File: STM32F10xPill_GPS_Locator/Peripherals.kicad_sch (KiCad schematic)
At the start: 0 parts

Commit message: Add controller and clocks
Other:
- company: (none) -> MTP
- title: (none) -> STM32F100C4T6B GPS Locator
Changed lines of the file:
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@@
 	(generator "eeschema")
 	(generator_version "9.0")
-	(paper "A4")
+	(paper "A3")
+	(title_block
+		(title "STM32F100C4T6B GPS Locator")
+		(date "2025-03-06")
+		(rev "1.0.0")
+		(company "MTP")
+	)
 )

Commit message: Add library parts for peripherals
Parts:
- added U2: QMC5883P, Package_LGA:LGA-16_3x3mm_P0.5mm, symbol ICs:QMC5883P
- added U4: ATGM336H-5N31, ICs:ATGM336H_SMD_9.7x10.1mm, symbol ICs:ATGM336H
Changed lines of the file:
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@@
 		(company "MTP")
 	)
+	(symbol
+		(lib_id "ICs:ATGM336H")
+		(at 257.81 135.89 0)
+		(unit 1)
+		(exclude_from_sim no)
+		(in_bom yes)
+		(on_board yes)
+		(dnp no)
+		(property "Reference" "U4"
+			(at 263.144 112.522 0)
+			(do_not_autoplace yes)
+			(effects
+				(font
+					(size 1.27 1.27)
+				)
+			)
+		)
+		(property "Value" "ATGM336H-5N31"
+			(at 268.732 114.3 0)
+			(effects
+				(font
+					(size 1.27 1.27)
+				)
+			)
+		)
+		(property "Footprint" "ICs:ATGM336H_SMD_9.7x10.1mm"
+			(at 257.81 135.89 0)
+			(effects
+				(font
+					(size 1.27 1.27)
+				)
+				(hide yes)
+			)
+		)
+		(property "Datasheet" ""
+			(at 257.81 135.89 0)
+			(effects
+				(font
+					(size 1.27 1.27)
+				)
+				(hide yes)
+			)
+		)
+		(property "Description" ""
+			(at 257.81 135.89 0)
+			(effects
+				(font
+					(size 1.27 1.27)
+				)
+				(hide yes)
+			)
+		)
+		(property "LCSC Part" "C90770"
+			(at 257.81 135.89 0)
+			(effects
+				(font
+					(size 1.27 1.27)
+				)
+				(hide yes)
+			)
+		)
+		(pin "9"
+		)
+		(pin "17"
+		)
+		(pin "8"
+		)
+		(pin "14"
+		)
+		(pin "16"
+		)
+		(pin "6"
+		)
+		(pin "4"
+		)
+		(pin "3"
+		)
+		(pin "1"
+		)
+		(pin "12"
+		)
+		(pin "11"
+		)
+		(pin "3"
+		)
+		(pin "2"
+		)
+		(pin "10"
+		)
+		(instances
+			(project ""
+				(path "/ea8b3ef8-8ecc-4b82-8187-a133f9b3c76f/fb7f8d9c-e54d-452d-9b35-e091bd157ab7"
+					(reference "U4")
+					(unit 1)
+				)
+			)
+		)
+	)
+	(symbol
+		(lib_id "ICs:QMC5883P")
+		(at 148.59 132.08 0)
+		(unit 1)
+		(exclude_from_sim no)
+		(in_bom yes)
+		(on_board yes)
+		(dnp no)
+		(property "Reference" "U2"
+			(at 153.67 118.872 0)
+			(effects
+				(font
+					(size 1.27 1.27)
+				)
+			)
+		)
+		(property "Value" "QMC5883P"
+			(at 156.972 120.65 0)
+			(effects
+				(font
+					(size 1.27 1.27)
+				)
+			)
+		)
+		(property "Footprint" "Package_LGA:LGA-16_3x3mm_P0.5mm"
+			(at 148.59 132.08 0)
+			(effects
+				(font
+					(size 1.27 1.27)
+				)
+				(hide yes)
+			)
+		)
+		(property "Datasheet" ""
+			(at 148.59 132.08 0)
+			(effects
+				(font
+					(size 1.27 1.27)
+				)
+				(hide yes)
+			)
+		)
+		(property "Description" ""
+			(at 148.59 132.08 0)
+			(effects
+				(font
+					(size 1.27 1.27)
+				)
+				(hide yes)
+			)
+		)
+		(property "LCSC Part" "C2847467"
+			(at 148.59 132.08 0)
+			(effects
+				(font
+					(size 1.27 1.27)
+				)
+				(hide yes)
+			)
+		)
+		(pin "11"
+		)
+		(pin "1"
+		)
+		(pin "9"
+		)
+		(pin "10"
+		)
+		(pin "2"
+		)
+		(pin "16"
+		)
+		(instances
+			(project ""
+				(path "/ea8b3ef8-8ecc-4b82-8187-a133f9b3c76f/fb7f8d9c-e54d-452d-9b35-e091bd157ab7"
+					(reference "U2")
+					(unit 1)
+				)
+			)
+		)
+	)
 )

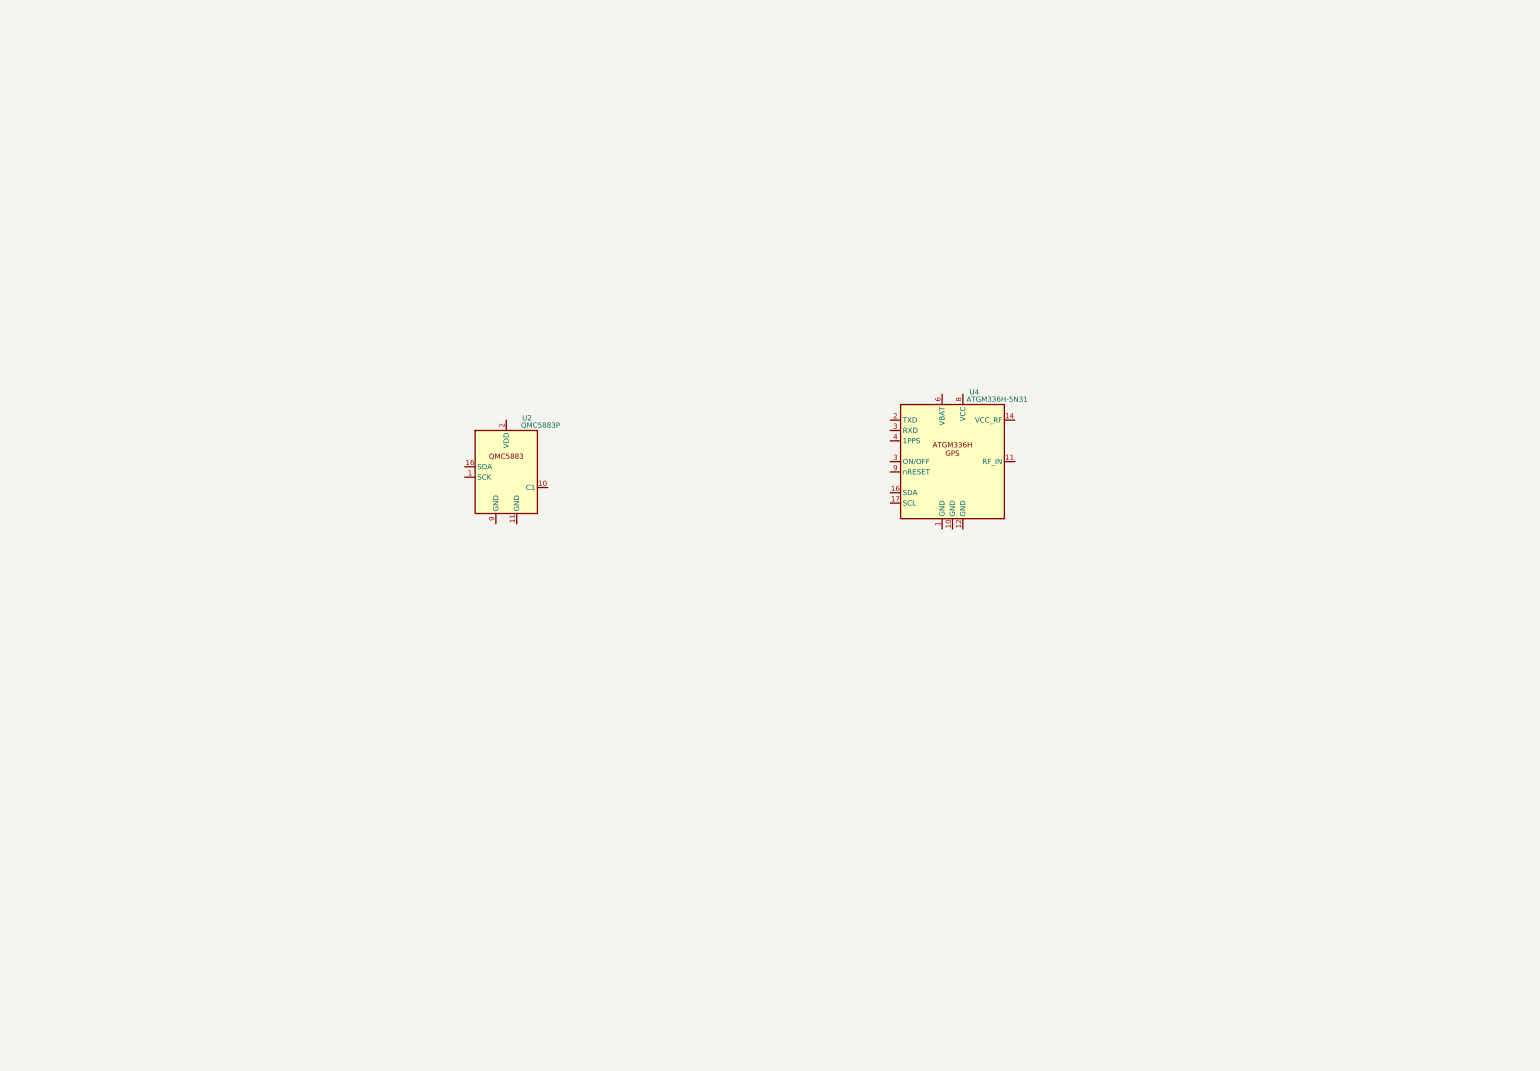
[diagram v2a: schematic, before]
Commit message: Work on adding GPS and Compass Peripherals
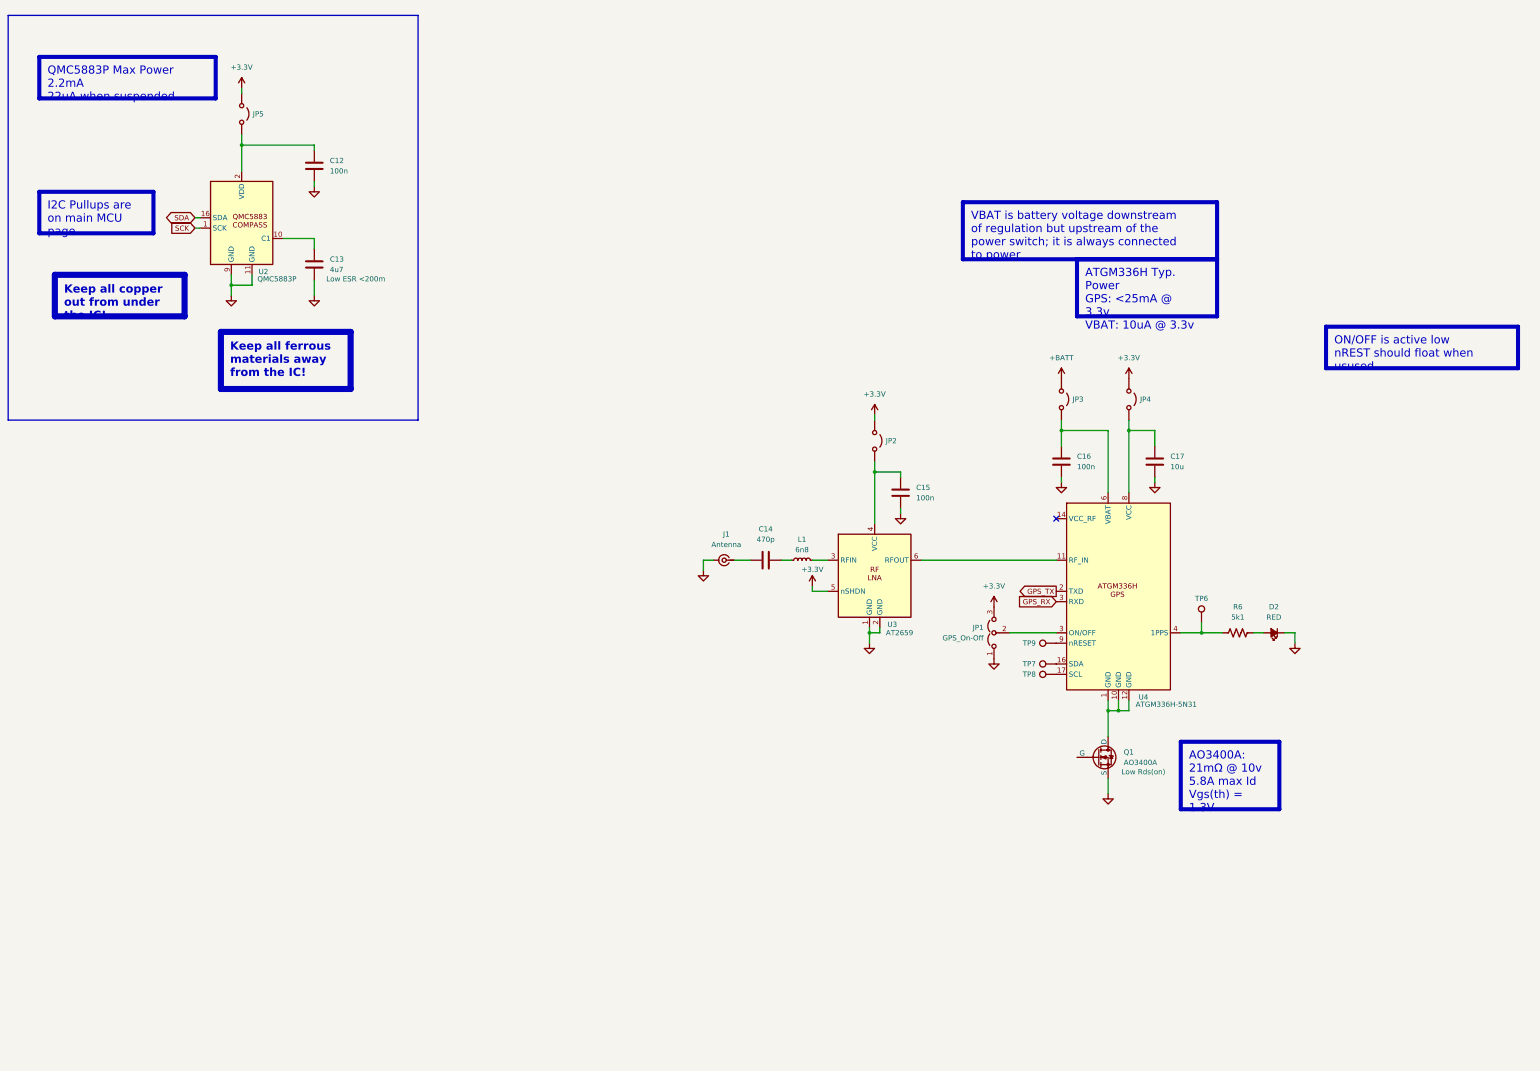
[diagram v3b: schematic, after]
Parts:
- added C12, C15, C16: 100n, symbol Device:C
- added C13: 4u7, symbol Device:C
- added C14: 470p, symbol Device:C
- added C17: 10u, symbol Device:C
- added D2: RED, symbol Device:LED_Small_Filled
- added J1: Antenna, Connector_Coaxial:U.FL_Molex_MCRF_73412-0110_Vertical, symbol Connector:Conn_Coaxial_Small
- added JP1: GPS_On-Off, symbol Jumper:Jumper_3_Open
- added JP2, JP3, JP4, JP5: Jumper_2_Open, symbol Jumper:Jumper_2_Open
- added L1: 6n8, symbol Device:L_Small
- added Q1: AO3400A, symbol Simulation_SPICE:NMOS
- added R6: 5k1, symbol Device:R_US
- added TP6: GPS_1PPS, symbol Connector:TestPoint
- added TP7, TP8: GPS_SDA, symbol Connector:TestPoint
- added TP9: GPS_nRESET, symbol Connector:TestPoint
- added U3: AT2659, Package_DFN_QFN:DFN-6_1.6x1.3mm_P0.4mm, symbol ICs:AT2659
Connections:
- net at U4.1 (GND): now also U4.10 (GND), U4.12 (GND), Q1.1 (D)
- net at U4.11 (RF_IN): now also U3.6 (RFOUT)
- net at U4.16 (SDA): now also TP7.1
- net at U4.17 (SCL): now also TP8.1
- net GPS_TX: now reaches U4.2 (TXD)
- net GPS_RX: now reaches U4.3 (ON/OFF)
- net at U4.4 (1PPS): now also R6.1, TP6.1
- net at U4.6 (VBAT): now also C16.2, JP3.2 (B)
- net at U4.8 (VCC): now also C17.2, JP4.2 (B)
- net at U4.9 (nRESET): now also TP9.1
- net SCK: now reaches U2.1 (SCK)
- net at U2.10 (C1): now also C13.2
- net GND: now reaches U2.11 (GND)
- net GND: now also U2.9 (GND), C12.1, C13.1, C15.1, C16.1, C17.1, D2.1 (K), J1.2 (Ext), JP1.1 (A), Q1.3 (S), U3.1 (GND), U3.2 (GND)
- net SDA: now reaches U2.16 (SDA)
- net at U2.2 (VDD): now also C12.2, JP5.2 (B)
- new net: C14.1, L1.2
- new net: C14.2, J1.1 (In)
- new net: D2.2 (A), R6.2
- new net: L1.1, U3.3 (RFIN)
- new net: C15.2, JP2.2 (B), U3.4 (VCC)
- new net: JP1.2 (C), U4.3 (ON/OFF)
- new net +3.3V: JP1.3 (B), JP2.1 (A), JP4.1 (A), JP5.1 (A), U3.5 (nSHDN)
- new net +BATT: JP3.1 (A)
- no-connect marks 0 -> 1
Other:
- moved on the sheet: U4

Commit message: Schematic is largely complete
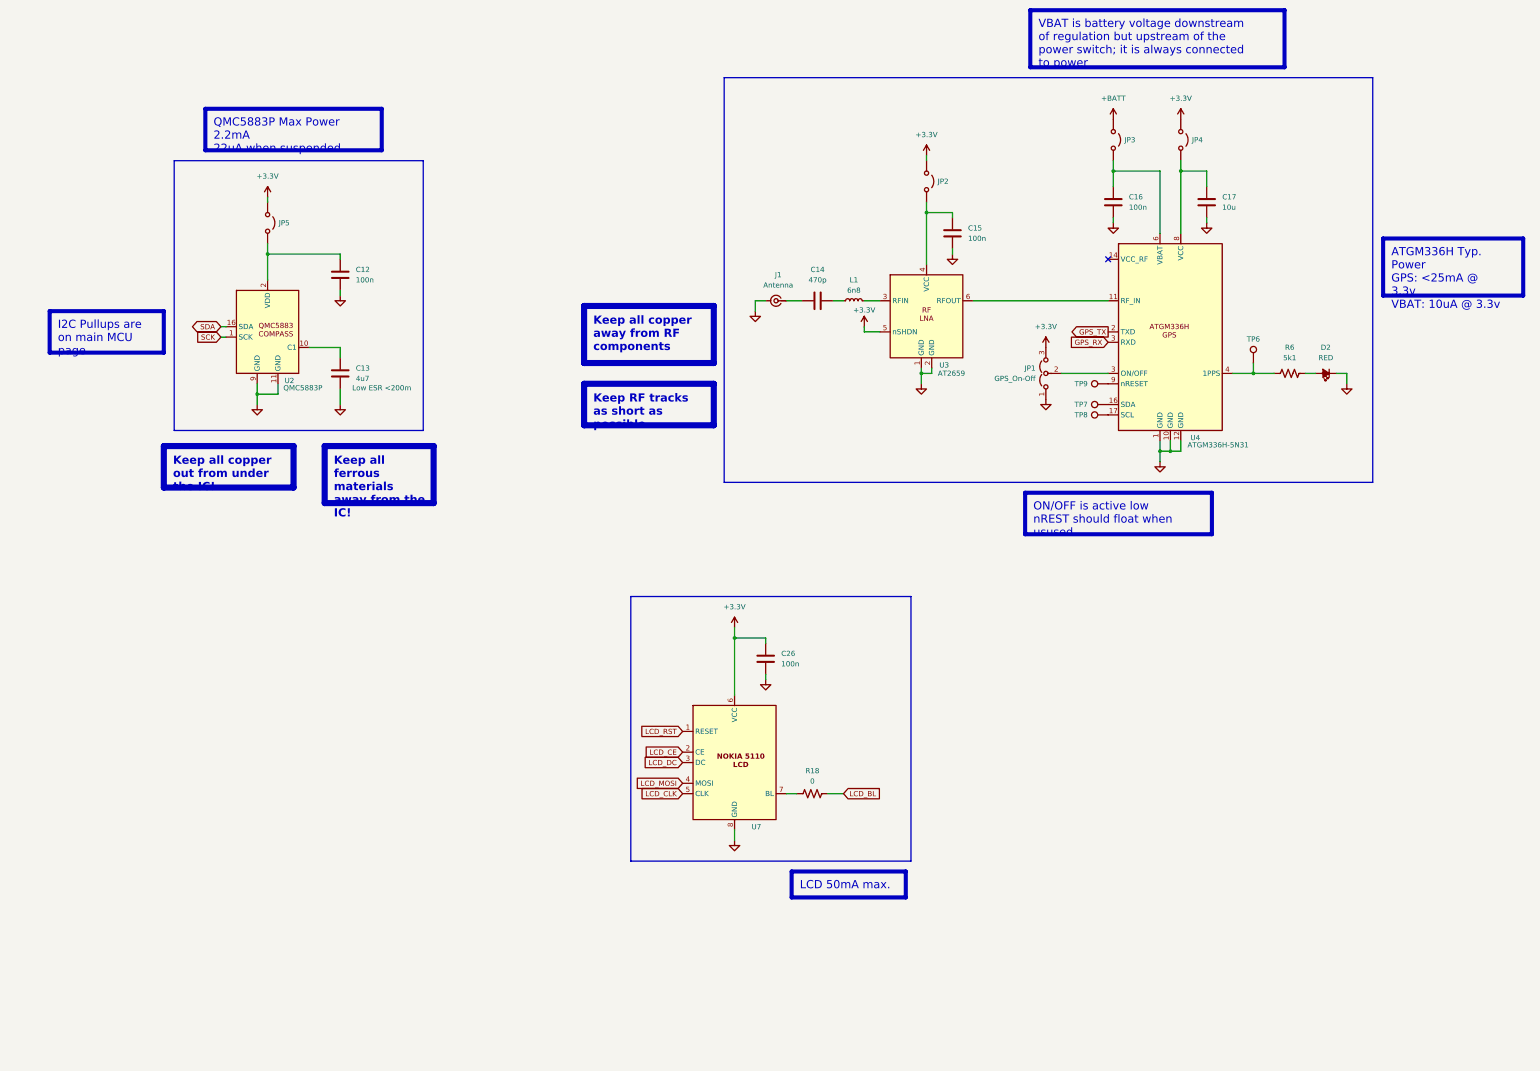
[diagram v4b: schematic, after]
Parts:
- removed Q1: AO3400A, symbol Simulation_SPICE:NMOS
- added C26: 100n, symbol Device:C
- added R18: 0, symbol Device:R_US
- added U7: ~, Connector_JST:JST_XH_B8B-XH-AM_1x08_P2.50mm_Vertical, symbol Modules:Nokia5110_LCD
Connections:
- net +3.3V: now also C26.2, U7.6 (VCC)
- net GND: now also U4.1 (GND), U4.10 (GND), U4.12 (GND), C26.1, U7.8 (GND)
- new net: R18.1, U7.7 (BL)
- new net LCD_BL: R18.2
- new net LCD_CE: U7.2 (CE)
- new net LCD_CLK: U7.5 (CLK)
- new net LCD_DC: U7.3 (DC)
- new net LCD_MOSI: U7.4 (MOSI)
- new net LCD_RST: U7.1 (RESET)
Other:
- moved on the sheet: C12, C13, C14, C15, C16, C17, D2, J1, JP1, JP2, JP3, JP4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

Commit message: Updated net names, submit schematic for feedback
After feedback is incorporated, PCB layout is ready to begin
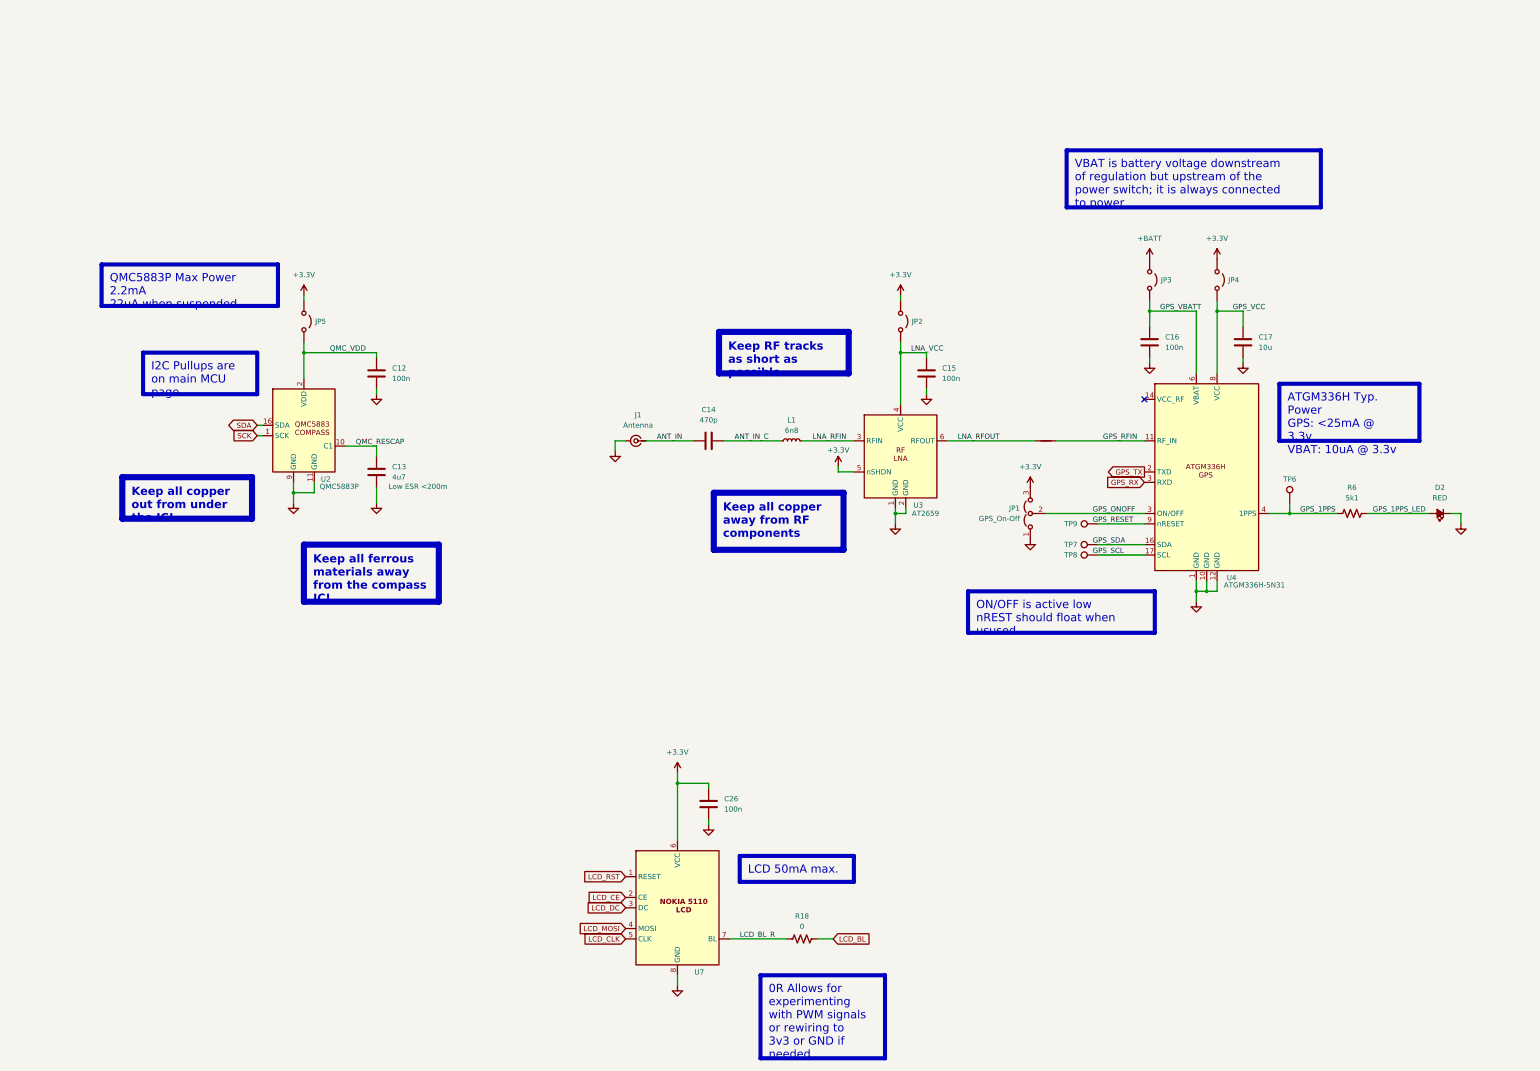
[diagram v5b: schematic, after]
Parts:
- added NT3: NetTie_2, NetTie:NetTie-2_SMD_Pad0.5mm, symbol Device:NetTie_2
- C12, C15, C16, C26: footprint (none) -> Capacitor_SMD:C_0603_1608Metric
- C13, C17: footprint (none) -> Capacitor_SMD:C_0805_2012Metric
- C14: footprint (none) -> Capacitor_SMD:C_0402_1005Metric
- D2: footprint (none) -> LED_SMD:LED_0603_1608Metric
- R18, R6: footprint (none) -> Resistor_SMD:R_0402_1005Metric_Pad0.72x0.64mm_HandSolder
- TP6, TP7, TP9: footprint (none) -> TestPoint:TestPoint_Pad_D1.5mm
- TP8: value GPS_SDA -> GPS_SCL; footprint (none) -> TestPoint:TestPoint_Pad_D1.5mm
- U7: footprint Connector_JST:JST_XH_B8B-XH-AM_1x08_P2.50mm_Vertical -> Connector_JST:JST_XH_B8B-XH-A_1x08_P2.50mm_Vertical
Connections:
- net LCD_BL_R: now reaches R18.1, U7.7 (BL)
- net ANT_IN_C: now reaches C14.1, L1.2
- net ANT_IN: now reaches C14.2, J1.1 (In)
- net GPS_VBATT: now reaches C16.2, JP3.2 (B), U4.6 (VBAT)
- net QMC_VDD: now reaches C12.2, JP5.2 (B), U2.2 (VDD)
- net GPS_VCC: now reaches C17.2, JP4.2 (B), U4.8 (VCC)
- net QMC_RESCAP: now reaches C13.2, U2.10 (C1)
- net GPS_1PPS: now reaches R6.1, TP6.1, U4.4 (1PPS)
- net GPS_1PPS_LED: now reaches D2.2 (A), R6.2
- net LNA_RFIN: now reaches L1.1, U3.3 (RFIN)
- net LNA_VCC: now reaches C15.2, JP2.2 (B), U3.4 (VCC)
- net GPS_RFIN: now reaches U4.11 (RF_IN)
- net GPS_RFIN: now also NT3.2; no longer U3.6 (RFOUT)
- net GPS_ONOFF: now reaches JP1.2 (C), U4.3 (ON/OFF)
- new net LNA_RFOUT: NT3.1, U3.6 (RFOUT)
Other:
- moved on the sheet: C12, C13, C14, C15, C16, C17, C26, D2, J1, JP1, JP2, JP3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
